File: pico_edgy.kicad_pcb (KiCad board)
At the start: 4 copper layers, 40 x 50.1 mm, 46 parts, among them J1 Conn_ARM_SWD_TagConnect_TC203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, J2 001, J3 002, J4 007, J5 100, J6 100, J7 USB_C_Receptacle_USB2.0_16P, SW1 boot, SW2 reset, U1 LM4040DBZ-3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

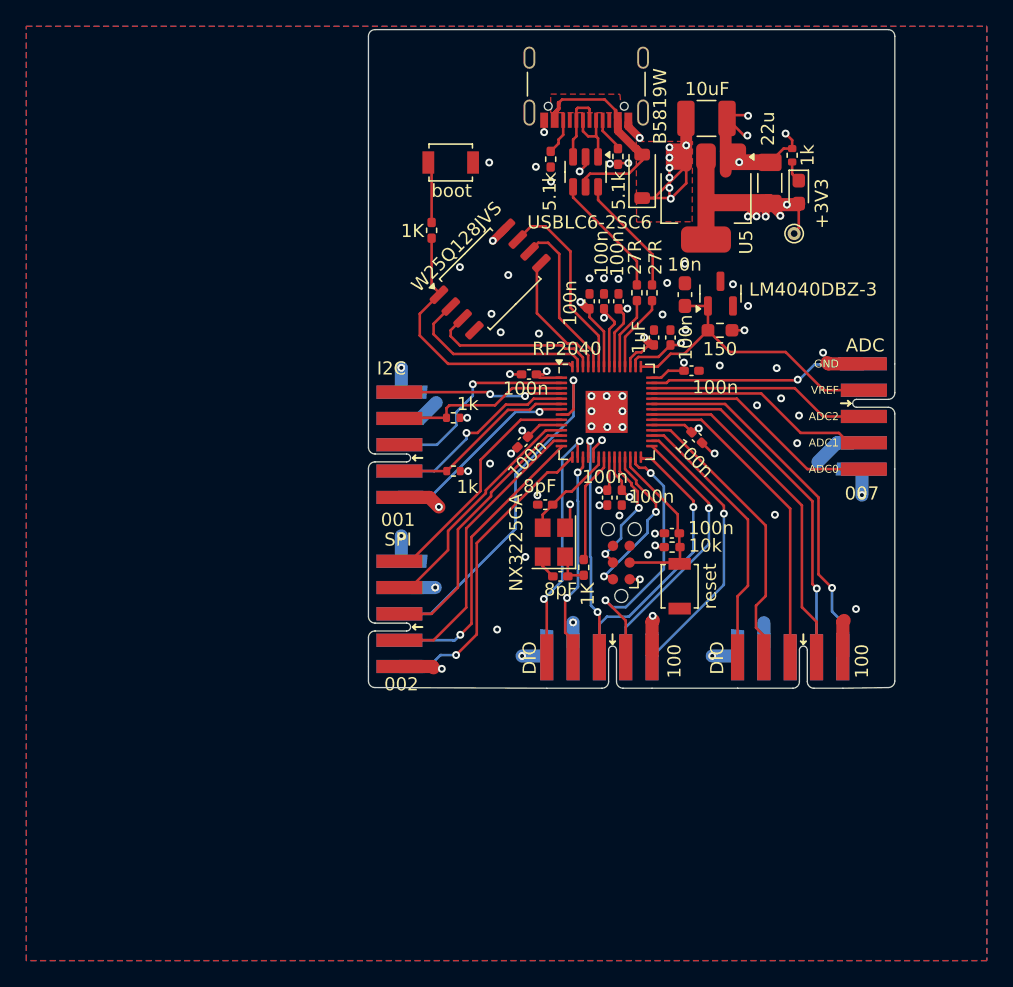
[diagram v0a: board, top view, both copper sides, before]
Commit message: layout from scratch, change some components to basic JLCPCB parts
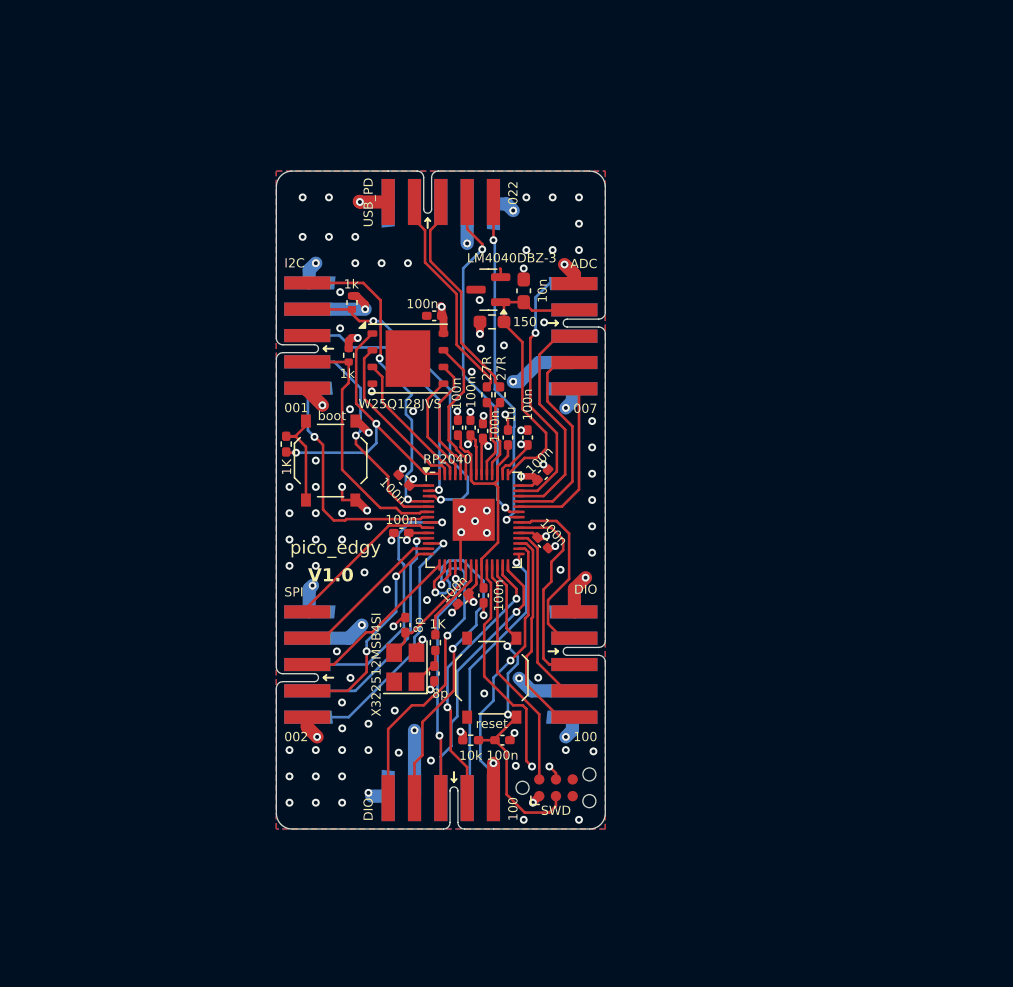
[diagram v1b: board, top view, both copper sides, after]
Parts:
- removed C17: 10uF, Capacitor_SMD:C_1210_3225Metric_Pad1.33x2.70mm_HandSolder
- removed C19: 22u, Capacitor_SMD:C_1206_3216Metric_Pad1.33x1.80mm_HandSolder
- removed D1: B5819W, Diode_SMD:D_SOD-123
- removed D2: +3V3, LED_SMD:LED_0603_1608Metric_Pad1.05x0.95mm_HandSolder
- removed J7: USB_C_Receptacle_USB2.0_16P, on_edge:USB_C_Receptacle_Palconn_UTC16-G
- removed R10, R9: 5.1k, Resistor_SMD:R_0402_1005Metric_Pad0.72x0.64mm_HandSolder
- removed R11: 1k, Resistor_SMD:R_0402_1005Metric
- removed TP1: +3V3, TestPoint:TestPoint_THTPad_D1.0mm_Drill0.5mm
- removed U4: USBLC6-2SC6, Package_TO_SOT_SMD:SOT-23-6
- removed U5: AMS1117-3.3, Package_TO_SOT_SMD:SOT-223-3_TabPin2
- added C9: 100n, Capacitor_SMD:C_0402_1005Metric_Pad0.74x0.62mm_HandSolder, F.Cu at (145.7, 101.5)
- added J8: 001, put_on_edge:on_edge_2x05_host, F.Cu at (136.0, 94.5)
- C3, C5: value 8pF -> 8p
- C8: value 1uF -> 1u
- J1: value Conn_ARM_SWD_TagConnect_TC2030-NL -> SWD
- J2: value 001 -> 002; footprint on_edge:on_edge_2x05_host -> put_on_edge:on_edge_2x05_host
- J3: value 002 -> 100; footprint on_edge:on_edge_2x05_host -> put_on_edge:on_edge_2x05_host
- J4, J5: footprint on_edge:on_edge_2x05_host -> put_on_edge:on_edge_2x05_host
- J6: value 100 -> 022; footprint on_edge:on_edge_2x05_host -> put_on_edge:on_edge_2x05_host
- SW1, SW2: footprint Button_Switch_SMD:SW_SPST_B3U-1000P -> Button_Switch_SMD:SW_Push_1P1T_XKB_TS-1187A
- U2: footprint Package_SO:SOIC-8_5.23x5.23mm_P1.27mm -> Package_SON:WSON-8-1EP_6x5mm_P1.27mm_EP3.4x4.3mm
- Y1: value NX3225GA -> X322512MSB4SI
- moved J6 49.8 mm to (144.5, 78.0), turned to 0 degrees
- moved SW1 24.4 mm to (140.1, 100.0), turned to -90 degrees
- moved J4 24.2 mm to (161.0, 86.5)
- moved J2 21.9 mm to (136.0, 119.5)
- moved R3 21.2 mm to (150.8, 121.2)
- moved C4 20.3 mm to (153.2, 121.2), turned to 0 degrees
- moved R1 19.6 mm to (136.8, 98.8)
- moved J3 18.9 mm to (152.5, 128.0), turned to 180 degrees
- moved C2 18.0 mm to (148.0, 89.0), turned to 180 degrees
- moved J1 17.8 mm to (157.2, 124.9), turned to 0 degrees
- moved C18 17.8 mm to (150.2, 110.5), turned to 45 degrees
- moved U1 17.6 mm to (152.1, 87.0), turned to 180 degrees
- moved C11 17.3 mm to (150.8, 97.5), turned to -90 degrees
- moved R2 17.3 mm to (152.4, 89.5), turned to 180 degrees
- moved C13 15.9 mm to (145.5, 105.5), turned to 0 degrees
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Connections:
- net /RP2040/ADC_VREF renamed /ADC_REF
- net /RP2040/GPIO26_ADC0 renamed /ADC2
- net /RP2040/GPIO27_ADC1 renamed /ADC1
- net /RP2040/GPIO28_ADC2 renamed /ADC0
- net /RP2040/GPIO29_ADC3 renamed /ADC3
- J2 pad 2: /SDA -> /SPI_MOSI
- J2 pad 3: unconnected-(J2-N/C-Pad3) -> /SPI_MISO
- J2 pad 4: /I2C0_SCL -> /SPI_SCLK
- J2 pad 5: /I2C_INT -> /SPI_INT
- J2 pad 6: /I2C_CS -> /SPI_CS
- J2 pad 7: /I2C_STATUS -> /SPI_STATUS
- J2 pad 8: /~{I2C_RESET} -> /~{SPI_RESET}
- J3 pad 2: /RP2040/GPIO10 -> /RP2040/GPIO16
- J3 pad 3: /RP2040/GPIO9 -> /RP2040/GPIO15
- J3 pad 4: /RP2040/GPIO8 -> /RP2040/GPIO14
- J3 pad 5: /RP2040/GPIO7 -> /RP2040/GPIO13
- J3 pad 6: /RP2040/GPIO12 -> /RP2040/GPIO19
- J3 pad 7: /RP2040/GPIO11 -> /RP2040/GPIO18
- J3 pad 8: /RP2040/GPIO6 -> /RP2040/GPIO17
- J4 pad 7: (no net) -> unconnected-(J4-NC-Pad7)
- J4 pad 8: (no net) -> unconnected-(J4-NC-Pad8)
- J5 pad 2: /RP2040/GPIO16 -> /RP2040/GPIO23
- J5 pad 3: /RP2040/GPIO15 -> /RP2040/GPIO22
- J5 pad 4: /RP2040/GPIO14 -> /RP2040/GPIO21
- J5 pad 5: /RP2040/GPIO13 -> /RP2040/GPIO20
- J5 pad 6: /RP2040/GPIO19 -> unconnected-(J5-IO4-Pad6)
- J5 pad 7: /RP2040/GPIO18 -> unconnected-(J5-IO5-Pad7)
- J5 pad 8: /RP2040/GPIO17 -> unconnected-(J5-IO6-Pad8)
- J6 pad 2: /RP2040/GPIO23 -> /RP2040/D+
- J6 pad 3: /RP2040/GPIO22 -> /RP2040/D-
- J6 pad 4: /RP2040/GPIO21 -> /RP2040/GPIO25
- J6 pad 5: /RP2040/GPIO20 -> /RP2040/GPIO24
- J6 pad 6: /RP2040/GPIO25 -> unconnected-(J6-NC-Pad6)
- J6 pad 7: /RP2040/GPIO24 -> unconnected-(J6-NC-Pad7)
- R7 pad 2: /SDA -> /I2C0_SDA
- U3 pad 11: /RP2040/GPIO8 -> /SPI_STATUS
- U3 pad 12: /RP2040/GPIO9 -> /SPI_CS
- U3 pad 13: /RP2040/GPIO10 -> /SPI_SCLK
- U3 pad 14: /RP2040/GPIO11 -> /SPI_MOSI
- U3 pad 15: /RP2040/GPIO12 -> /SPI_MISO
- U3 pad 2: /~{I2C_RESET} -> /~{I2C0_RESET}
- U3 pad 4: /I2C_INT -> /I2C0_INT
- U3 pad 5: /I2C_STATUS -> /I2C0_STATUS
- U3 pad 6: /SDA -> /I2C0_SDA
- U3 pad 7: /I2C_CS -> /I2C0_CS
- U3 pad 8: /RP2040/GPIO6 -> /~{SPI_RESET}
- U3 pad 9: /RP2040/GPIO7 -> /SPI_INT
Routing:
- net /RP2040/GPIO6: track 27.9 -> 0.00 mm, vias 1 -> 0
- net +3V3: track 85.9 -> 60.6 mm, vias 22 -> 19
- net /I2C0_INT: track 0.00 -> 24.5 mm, vias 0 -> 2
- net /RP2040/GPIO12: track 23.8 -> 0.00 mm, vias 1 -> 0
- net /RP2040/GPIO11: track 22.4 -> 0.00 mm, vias 1 -> 0
- net /RP2040/GPIO10: track 22.1 -> 0.00 mm
- net /RP2040/GPIO9: track 20.7 -> 0.00 mm
- net /~{SPI_RESET}: track 0.00 -> 20.5 mm, vias 0 -> 1
- net /SPI_CS: track 0.00 -> 20.4 mm, vias 0 -> 1
- net /~{I2C0_RESET}: track 0.00 -> 19.8 mm, vias 0 -> 1
- net /I2C0_SDA: track 0.00 -> 19.5 mm
- net +5V: track 30.6 -> 11.3 mm, vias 12 -> 6
- net /RP2040/GPIO8: track 18.2 -> 0.00 mm
- net /I2C0_CS: track 0.00 -> 18.2 mm, vias 0 -> 1
- net /RP2040/GPIO7: track 18.1 -> 0.00 mm
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- added copper zone on In2.Cu, net +3V3
- added copper zone on B.Cu, net GND
- removed copper zone on B.Cu, net +3V3
- removed copper zone on F.Cu, net +5V
- removed copper zone on F.Cu, net VBUS
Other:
- board size 40 x 50.1 mm -> 25 x 50 mm
- board text added: "V1.0"
- board text added: "pico_edgy"
- board text removed: "+3V3"
- board text removed: "+5V"
- board text removed: "ADC0"
- board text removed: "ADC1"
- board text removed: "ADC2"
- board text removed: "ADC3"
- board text removed: "GND"
- board text removed: "VREF"
